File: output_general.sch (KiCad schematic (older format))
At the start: 13 parts

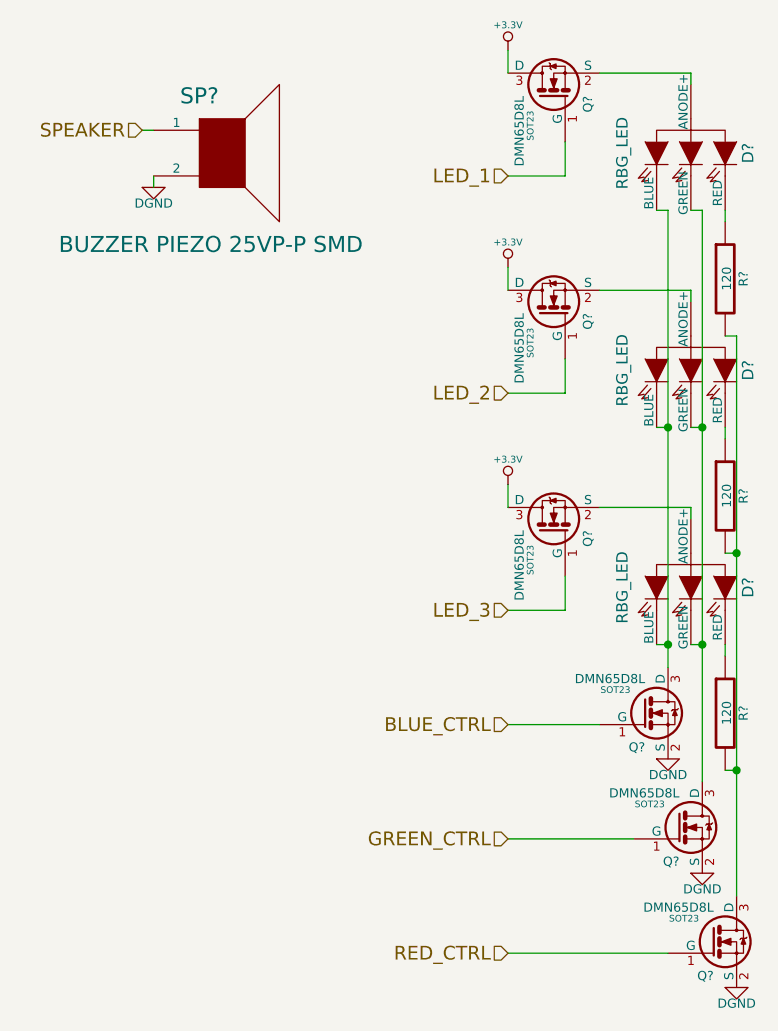
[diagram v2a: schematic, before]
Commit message: various fixes due to issues found in ERC
learned how to use invisible pins
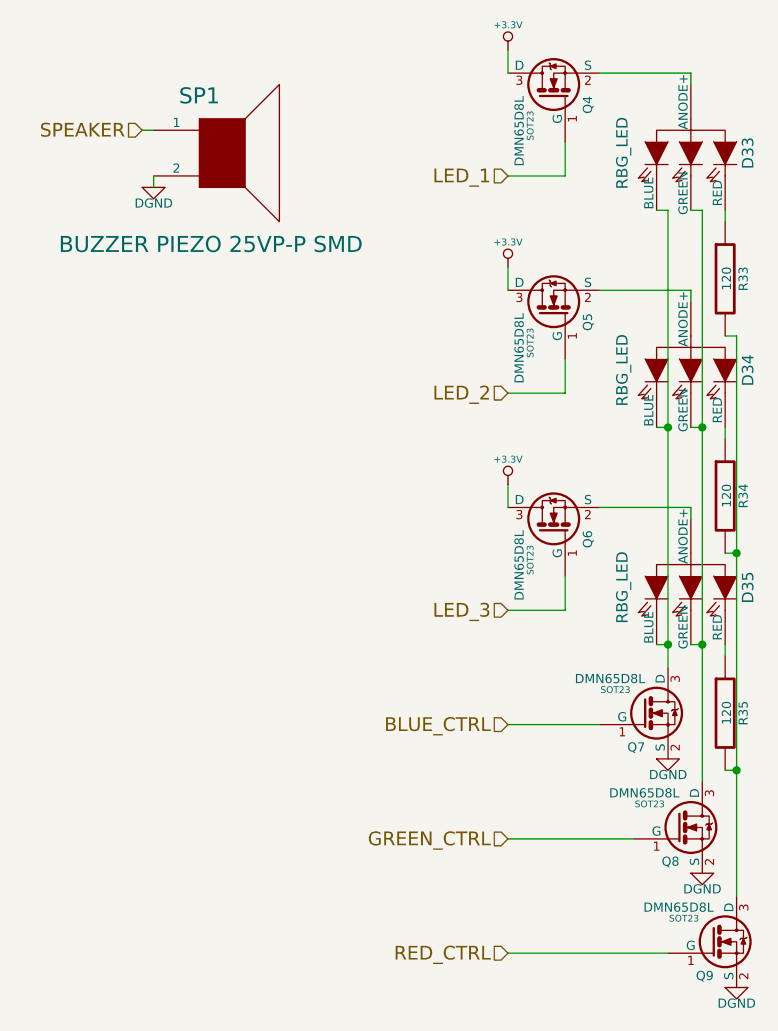
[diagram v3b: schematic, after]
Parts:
- gave numbers to parts that had none: 13
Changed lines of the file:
@@
 Sheet 12 18
 Title ""
-Date "18 dec 2013"
+Date "20 dec 2013"
 Rev ""
 Comp ""
@@
 $EndDescr
 $Comp
-L SPEAKER SP?
+L SPEAKER SP1
 U 1 1 52803375
 P 1350 1100
-F 0 "SP?" H 1250 1350 70  0000 C CNN
+F 0 "SP1" H 1250 1350 70  0000 C CNN
 F 1 "BUZZER PIEZO 25VP-P SMD" H 1300 700 70  0000 C CNN
 F 2 "~" H 1350 1100 60  0000 C CNN
@@
 $EndComp
 $Comp
-L DGND #PWR?
+L DGND #PWR066
 U 1 1 528035E5
 P 1050 1250
-F 0 "#PWR?" H 1050 1250 40  0001 C CNN
+F 0 "#PWR066" H 1050 1250 40  0001 C CNN
 F 1 "DGND" H 1050 1180 40  0000 C CNN
 F 2 "" H 1050 1250 60  0000 C CNN
@@
 SPEAKER
 $Comp
-L R R?
+L R R33
 U 1 1 52803610
 P 3550 1650
-F 0 "R?" V 3630 1650 40  0000 C CNN
+F 0 "R33" V 3630 1650 40  0000 C CNN
 F 1 "120" V 3557 1651 40  0000 C CNN
 F 2 "~" V 3480 1650 30  0000 C CNN
@@
 $EndComp
 $Comp
-L R R?
+L R R34
 U 1 1 52803622
 P 3550 2600
-F 0 "R?" V 3630 2600 40  0000 C CNN
+F 0 "R34" V 3630 2600 40  0000 C CNN
 F 1 "120" V 3557 2601 40  0000 C CNN
 F 2 "~" V 3480 2600 30  0000 C CNN
@@
 $EndComp
 $Comp
-L R R?
+L R R35
 U 1 1 5280362D
 P 3550 3550
-F 0 "R?" V 3630 3550 40  0000 C CNN
+F 0 "R35" V 3630 3550 40  0000 C CNN
 F 1 "120" V 3557 3551 40  0000 C CNN
 F 2 "~" V 3480 3550 30  0000 C CNN
@@
 $EndComp
 $Comp
-L DMN65D8L Q?
+L DMN65D8L Q7
 U 1 1 528037B6
 P 3200 3550
-F 0 "Q?" H 3200 3401 40  0000 R CNN
+F 0 "Q7" H 3200 3401 40  0000 R CNN
 F 1 "DMN65D8L" H 3200 3700 40  0000 R CNN
 F 2 "SOT23" H 3070 3652 29  0000 C CNN
@@
 $EndComp
 $Comp
-L DMN65D8L Q?
+L DMN65D8L Q9
 U 1 1 528037C3
 P 3500 4550
-F 0 "Q?" H 3500 4401 40  0000 R CNN
+F 0 "Q9" H 3500 4401 40  0000 R CNN
 F 1 "DMN65D8L" H 3500 4700 40  0000 R CNN
 F 2 "SOT23" H 3370 4652 29  0000 C CNN
@@
 $EndComp
 $Comp
-L DMN65D8L Q?
+L DMN65D8L Q8
 U 1 1 528037C9
 P 3350 4050
-F 0 "Q?" H 3350 3901 40  0000 R CNN
+F 0 "Q8" H 3350 3901 40  0000 R CNN
 F 1 "DMN65D8L" H 3350 4200 40  0000 R CNN
 F 2 "SOT23" H 3220 4152 29  0000 C CNN
@@
 $EndComp
 $Comp
-L RBG_LED D?
+L RBG_LED D35
 U 1 1 52803F28
 P 3400 3000
-F 0 "D?" H 3400 3250 50  0000 C CNN
+F 0 "D35" H 3400 3250 50  0000 C CNN
 F 1 "RBG_LED" H 3400 2700 50  0000 C CNN
 F 2 "~" H 3400 2850 60  0000 C CNN
@@
 $EndComp
 $Comp
-L RBG_LED D?
+L RBG_LED D33
 U 1 1 52803F35
 P 3400 1100
-F 0 "D?" H 3400 1350 50  0000 C CNN
+F 0 "D33" H 3400 1350 50  0000 C CNN
 F 1 "RBG_LED" H 3400 800 50  0000 C CNN
 F 2 "~" H 3400 950 60  0000 C CNN
@@
 $EndComp
 $Comp
-L RBG_LED D?
+L RBG_LED D34
 U 1 1 52803F45
 P 3400 2050
-F 0 "D?" H 3400 2300 50  0000 C CNN
+F 0 "D34" H 3400 2300 50  0000 C CNN
 F 1 "RBG_LED" H 3400 1750 50  0000 C CNN
 F 2 "~" H 3400 1900 60  0000 C CNN
@@
 $EndComp
 $Comp
-L DMN65D8L Q?
+L DMN65D8L Q6
 U 1 1 52804046
 P 2800 2750
-F 0 "Q?" H 2800 2601 40  0000 R CNN
+F 0 "Q6" H 2800 2601 40  0000 R CNN
 F 1 "DMN65D8L" H 2800 2900 40  0000 R CNN
 F 2 "SOT23" H 2670 2852 29  0000 C CNN
@@
 $EndComp
 $Comp
-L DMN65D8L Q?
+L DMN65D8L Q5
 U 1 1 5280404C
 P 2800 1800
-F 0 "Q?" H 2800 1651 40  0000 R CNN
+F 0 "Q5" H 2800 1651 40  0000 R CNN
 F 1 "DMN65D8L" H 2800 1950 40  0000 R CNN
 F 2 "SOT23" H 2670 1902 29  0000 C CNN
@@
 $EndComp
 $Comp
-L DMN65D8L Q?
+L DMN65D8L Q4
 U 1 1 52804052
 P 2800 850
-F 0 "Q?" H 2800 701 40  0000 R CNN
+F 0 "Q4" H 2800 701 40  0000 R CNN
 F 1 "DMN65D8L" H 2800 1000 40  0000 R CNN
 F 2 "SOT23" H 2670 952 29  0000 C CNN
@@
 $EndComp
 $Comp
-L DGND #PWR?
+L DGND #PWR067
 U 1 1 528040AE
 P 3300 3750
-F 0 "#PWR?" H 3300 3750 40  0001 C CNN
+F 0 "#PWR067" H 3300 3750 40  0001 C CNN
 F 1 "DGND" H 3300 3680 40  0000 C CNN
 F 2 "" H 3300 3750 60  0000 C CNN
@@
 $EndComp
 $Comp
-L DGND #PWR?
+L DGND #PWR068
 U 1 1 528040B4
 P 3450 4250
-F 0 "#PWR?" H 3450 4250 40  0001 C CNN
+F 0 "#PWR068" H 3450 4250 40  0001 C CNN
 F 1 "DGND" H 3450 4180 40  0000 C CNN
 F 2 "" H 3450 4250 60  0000 C CNN
@@
 $EndComp
 $Comp
-L DGND #PWR?
+L DGND #PWR069
 U 1 1 528040BA
 P 3600 4750
-F 0 "#PWR?" H 3600 4750 40  0001 C CNN
+F 0 "#PWR069" H 3600 4750 40  0001 C CNN
 F 1 "DGND" H 3600 4680 40  0000 C CNN
 F 2 "" H 3600 4750 60  0000 C CNN
@@
 $EndComp
 $Comp
-L +3.3V #PWR?
+L +3.3V #PWR070
 U 1 1 52804204
 P 2600 650
-F 0 "#PWR?" H 2600 610 30  0001 C CNN
+F 0 "#PWR070" H 2600 610 30  0001 C CNN
 F 1 "+3.3V" H 2600 760 30  0000 C CNN
 F 2 "" H 2600 650 60  0000 C CNN
@@
 	2600 650  2600 750
 $Comp
-L +3.3V #PWR?
+L +3.3V #PWR071
 U 1 1 52804290
 P 2600 1600
-F 0 "#PWR?" H 2600 1560 30  0001 C CNN
+F 0 "#PWR071" H 2600 1560 30  0001 C CNN
 F 1 "+3.3V" H 2600 1710 30  0000 C CNN
 F 2 "" H 2600 1600 60  0000 C CNN
@@
 $EndComp
 $Comp
-L +3.3V #PWR?
+L +3.3V #PWR072
 U 1 1 52804296
 P 2600 2550
-F 0 "#PWR?" H 2600 2510 30  0001 C CNN
+F 0 "#PWR072" H 2600 2510 30  0001 C CNN
 F 1 "+3.3V" H 2600 2660 30  0000 C CNN
 F 2 "" H 2600 2550 60  0000 C CNN

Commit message: placed components ... quite the task!
there is a lot of shit going on in this board... :D
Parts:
- renumbered D33 to D7, D34 to D8, D35 to D9, R33 to R28, R34 to R29, R35 to R30
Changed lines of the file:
@@
 $Descr A4 11693 8268
 encoding utf-8
-Sheet 12 18
+Sheet 12 15
 Title ""
-Date "12 jan 2014"
+Date "18 jan 2014"
 Rev ""
 Comp ""
@@
 $EndComp
 $Comp
-L DGND #PWR068
+L DGND #PWR059
 U 1 1 528035E5
 P 1050 1250
-F 0 "#PWR068" H 1050 1250 40  0001 C CNN
+F 0 "#PWR059" H 1050 1250 40  0001 C CNN
 F 1 "DGND" H 1050 1180 40  0000 C CNN
 F 2 "" H 1050 1250 60  0000 C CNN
@@
 SPEAKER
 $Comp
-L R R33
+L R R28
 U 1 1 52803610
 P 3550 1650
-F 0 "R33" V 3630 1650 40  0000 C CNN
+F 0 "R28" V 3630 1650 40  0000 C CNN
 F 1 "120" V 3557 1651 40  0000 C CNN
 F 2 "~" V 3480 1650 30  0000 C CNN
@@
 $EndComp
 $Comp
-L R R34
+L R R29
 U 1 1 52803622
 P 3550 2600
-F 0 "R34" V 3630 2600 40  0000 C CNN
+F 0 "R29" V 3630 2600 40  0000 C CNN
 F 1 "120" V 3557 2601 40  0000 C CNN
 F 2 "~" V 3480 2600 30  0000 C CNN
@@
 $EndComp
 $Comp
-L R R35
+L R R30
 U 1 1 5280362D
 P 3550 3550
-F 0 "R35" V 3630 3550 40  0000 C CNN
+F 0 "R30" V 3630 3550 40  0000 C CNN
 F 1 "120" V 3557 3551 40  0000 C CNN
 F 2 "~" V 3480 3550 30  0000 C CNN
@@
 $EndComp
 $Comp
-L RBG_LED D35
+L RBG_LED D9
 U 1 1 52803F28
 P 3400 3000
-F 0 "D35" H 3400 3250 50  0000 C CNN
+F 0 "D9" H 3400 3250 50  0000 C CNN
 F 1 "RBG_LED" H 3400 2700 50  0000 C CNN
 F 2 "~" H 3400 2850 60  0000 C CNN
@@
 $EndComp
 $Comp
-L RBG_LED D33
+L RBG_LED D7
 U 1 1 52803F35
 P 3400 1100
-F 0 "D33" H 3400 1350 50  0000 C CNN
+F 0 "D7" H 3400 1350 50  0000 C CNN
 F 1 "RBG_LED" H 3400 800 50  0000 C CNN
 F 2 "~" H 3400 950 60  0000 C CNN
@@
 $EndComp
 $Comp
-L RBG_LED D34
+L RBG_LED D8
 U 1 1 52803F45
 P 3400 2050
-F 0 "D34" H 3400 2300 50  0000 C CNN
+F 0 "D8" H 3400 2300 50  0000 C CNN
 F 1 "RBG_LED" H 3400 1750 50  0000 C CNN
 F 2 "~" H 3400 1900 60  0000 C CNN
@@
 $EndComp
 $Comp
-L DGND #PWR069
+L DGND #PWR060
 U 1 1 528040AE
 P 3300 3750
-F 0 "#PWR069" H 3300 3750 40  0001 C CNN
+F 0 "#PWR060" H 3300 3750 40  0001 C CNN
 F 1 "DGND" H 3300 3680 40  0000 C CNN
 F 2 "" H 3300 3750 60  0000 C CNN
@@
 $EndComp
 $Comp
-L DGND #PWR070
+L DGND #PWR061
 U 1 1 528040B4
 P 3450 4250
-F 0 "#PWR070" H 3450 4250 40  0001 C CNN
+F 0 "#PWR061" H 3450 4250 40  0001 C CNN
 F 1 "DGND" H 3450 4180 40  0000 C CNN
 F 2 "" H 3450 4250 60  0000 C CNN
@@
 $EndComp
 $Comp
-L DGND #PWR071
+L DGND #PWR062
 U 1 1 528040BA
 P 3600 4750
-F 0 "#PWR071" H 3600 4750 40  0001 C CNN
+F 0 "#PWR062" H 3600 4750 40  0001 C CNN
 F 1 "DGND" H 3600 4680 40  0000 C CNN
 F 2 "" H 3600 4750 60  0000 C CNN
@@
 $EndComp
 $Comp
-L +3.3V #PWR072
+L +3.3V #PWR063
 U 1 1 52804204
 P 2600 650
-F 0 "#PWR072" H 2600 610 30  0001 C CNN
+F 0 "#PWR063" H 2600 610 30  0001 C CNN
 F 1 "+3.3V" H 2600 760 30  0000 C CNN
 F 2 "" H 2600 650 60  0000 C CNN
@@
 	2600 650  2600 750
 $Comp
-L +3.3V #PWR073
+L +3.3V #PWR064
 U 1 1 52804290
 P 2600 1600
-F 0 "#PWR073" H 2600 1560 30  0001 C CNN
+F 0 "#PWR064" H 2600 1560 30  0001 C CNN
 F 1 "+3.3V" H 2600 1710 30  0000 C CNN
 F 2 "" H 2600 1600 60  0000 C CNN
@@
 $EndComp
 $Comp
-L +3.3V #PWR074
+L +3.3V #PWR065
 U 1 1 52804296
 P 2600 2550
-F 0 "#PWR074" H 2600 2510 30  0001 C CNN
+F 0 "#PWR065" H 2600 2510 30  0001 C CNN
 F 1 "+3.3V" H 2600 2660 30  0000 C CNN
 F 2 "" H 2600 2550 60  0000 C CNN
